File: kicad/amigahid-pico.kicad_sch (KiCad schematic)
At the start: 57 parts, among them J1 Amiga keyboard connector, J2 Conn_02x05_Top_Bottom, J3 Conn_02x05_Top_Bottom, J4 Conn_01x06, J5 Conn_01x04, Q1 BSS138, Q10 BSS138, Q11 BSS138, Q12 BSS138, Q13 BSS138, Q14 BSS138, Q15 BSS138, Q16 BSS138, Q17 BSS138, Q2 BSS138, Q3 BSS138, Q4 BSS138, Q5 BSS138, Q6 BSS138, Q7 BSS138, Q8 BSS138, Q9 BSS138, U1 Pico

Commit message: change resistor footprints to 1608 (metric)
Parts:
- R1, R10, R11, R12, R13, R14, R15, R16, R17, R18, R19, R2, R20, R21, R22, R23, R24, R25, R26, R27, R28, R29, R3, R30, R31, R32, R33, R34, R4, R5, R6, R7, R8, R9: footprint Resistor_SMD:R_0201_0603Metric -> Resistor_SMD:R_0603_1608Metric

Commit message: pcb rev 4
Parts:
- removed J2, J3: Conn_02x05_Top_Bottom, Connector_IDC:IDC-Header_2x05_P2.54mm_Vertical, symbol Connector_Generic:Conn_02x05_Top_Bottom
- removed J4: Conn_01x06, Connector_PinHeader_2.54mm:PinHeader_1x06_P2.54mm_Horizontal, symbol Connector_Generic:Conn_01x06
- removed J5: Conn_01x04, Connector_PinSocket_2.54mm:PinSocket_1x04_P2.54mm_Vertical, symbol Connector_Generic:Conn_01x04
- added J2: Debug/programming, Connector_PinHeader_2.54mm:PinHeader_1x06_P2.54mm_Horizontal, symbol Connector_Generic:Conn_01x06
- added J3: i2c header, Connector_PinHeader_2.54mm:PinHeader_1x04_P2.54mm_Vertical, symbol Connector_Generic:Conn_01x04
- added J4: USB_A, Connector_USB:USB_A_Molex_67643_Horizontal, symbol Connector:USB_A
- added J5: Controller 1, Connector_IDC:IDC-Header_2x05_P2.54mm_Vertical, symbol Connector_Generic:Conn_02x05_Odd_Even
- added J6: Controller 2, Connector_IDC:IDC-Header_2x05_P2.54mm_Vertical, symbol Connector_Generic:Conn_02x05_Odd_Even
- J1: value Amiga keyboard connector -> Amiga Keyboard
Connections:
- net +5V: now also R1.2, R11.2, R13.2, R15.2, R17.2, R19.2, R21.2, R23.2, R25.2, R27.2, R29.2, R3.2, R31.2, R33.2, R5.2, R7.2, R9.2, J4.1 (VBUS); no longer R1.1, R10.1, R12.1, R14.1, R16.1, R18.1, R20.1, R22.1, R24.1, R26.1, R28.1, R3.1, R30.1, R32.1, R34.1, R5.1, R8.1
- net kbclock: now reaches J1.1 (Pin_1), Q1.3 (D)
- net kbclock: now also R1.1; no longer R1.2
- net kbdata: now reaches J1.2 (Pin_2), Q2.3 (D)
- net kbdata: now also R3.1; no longer R3.2
- net kbreset: now reaches J1.3 (Pin_3), Q3.3 (D)
- net kbreset: now also R5.1; no longer R5.2
- net GND: now reaches J1.6 (Pin_6), U1.13 (GND), U1.18 (GND), U1.23 (GND), U1.28 (GND), U1.3 (GND), U1.33 (AGND), U1.38 (GND), U1.42 (GND), U1.8 (GND)
- net GND: now also J2.1 (Pin_1), J2.5 (Pin_5), J3.2 (Pin_2), J4.4 (GND), J4.5 (Shield), J5.6 (Pin_6), J6.6 (Pin_6)
- net kbpowerled: now reaches J1.7 (Pin_7)
- net kbdriveled: now reaches J1.8 (Pin_8)
- net uart tx: now reaches U1.1 (GPIO0)
- net uart tx: now also J2.2 (Pin_2)
- net lcont1 b3: now reaches U1.17 (GPIO13)
- net lcont1 b3: now also Q10.2 (S), R20.1
- net uart rx: now reaches U1.2 (GPIO1)
- net uart rx: now also J2.3 (Pin_3)
- net lcont2 h: now reaches U1.30 (RUN)
- net lcont2 h: now also Q12.2 (S), R24.1
- net +3V3: now reaches Q1.1 (G), Q10.1 (G), Q11.1 (G), Q12.1 (G), Q13.1 (G), Q14.1 (G), Q15.1 (G), Q16.1 (G), Q17.1 (G), Q2.1 (G), Q3.1 (G), Q4.1 (G), Q5.1 (G), Q6.1 (G), Q7.1 (G), Q8.1 (G), Q9.1 (G), U1.36 (3V3)
- net +3V3: now also R10.2, R12.2, R14.2, R16.2, R18.2, R2.2, R20.2, R22.2, R24.2, R26.2, R28.2, R30.2, R32.2, R34.2, R4.2, R6.2, R8.2, J3.1 (Pin_1); no longer R11.1, R13.1, R15.1, R17.1, R19.1, R2.1, R21.1, R23.1, R25.1, R27.1, R29.1, R31.1, R33.1, R4.1, R6.1, R7.1, R9.1
- net i2c sda: now reaches U1.4 (GPIO2)
- net i2c sda: now also J3.4 (Pin_4)
- net swclk: now reaches U1.41 (SWCLK)
- net swclk: now also J2.6 (Pin_6)
- net swdio: now reaches U1.43 (SWDIO)
- net swdio: now also J2.4 (Pin_4)
- net i2c scl: now reaches U1.5 (GPIO3)
- net i2c scl: now also J3.3 (Pin_3)
- net lkbreset: now reaches U1.6 (GPIO4)
- net lkbreset: now also Q3.2 (S), R6.1
- net lkbdata: now reaches U1.7 (GPIO5)
- net lkbdata: now also Q2.2 (S), R4.1
- net cont2 v: now reaches Q11.3 (D)
- net cont2 v: now also R21.1, J6.1 (Pin_1); no longer R22.2
- net cont2 b1: now reaches Q15.3 (D)
- net cont2 b1: now also R29.1, J6.2 (Pin_2); no longer R30.2
- net cont2 b2: now reaches Q16.3 (D)
- net cont2 b2: now also R31.1, J6.8 (Pin_8); no longer R32.2
- net cont1 b1: now reaches Q8.3 (D)
- net cont1 b1: now also R15.1, J5.2 (Pin_2); no longer R16.2
- net cont1 v: now reaches Q7.3 (D)
- net cont1 v: now also R13.1, J5.1 (Pin_1); no longer R14.2
- net cont1 h: now reaches Q6.3 (D)
- net cont1 h: now also R11.1, J5.3 (Pin_3); no longer R12.2
- net cont1 vq: now reaches Q5.3 (D)
- net cont1 vq: now also R9.1, J5.5 (Pin_5); no longer R10.2
- net cont1 hq: now reaches Q4.3 (D)
- net cont1 hq: now also R7.1, J5.7 (Pin_7); no longer R8.2
- net cont1 b2: now reaches Q9.3 (D)
- net cont1 b2: now also R17.1, J5.8 (Pin_8); no longer R18.2
- net cont1 b3: now reaches Q10.3 (D)
- net cont1 b3: now also R19.1, J5.9 (Pin_9); no longer R20.2
- net cont2 h: now reaches Q12.3 (D)
- net cont2 h: now also R23.1, J6.3 (Pin_3); no longer R24.2
- net cont2 b3: now reaches Q17.3 (D)
- net cont2 b3: now also R33.1, J6.9 (Pin_9); no longer R34.2
- net cont2 vq: now reaches Q13.3 (D)
- net cont2 vq: now also R25.1, J6.5 (Pin_5); no longer R26.2
- net cont2 hq: now reaches Q14.3 (D)
- net cont2 hq: now also R27.1, J6.7 (Pin_7); no longer R28.2
- new net lcont1 b1: Q8.2 (S), R16.1, U1.15 (GPIO11)
- new net lcont1 b2: Q9.2 (S), R18.1, U1.16 (GPIO12)
- new net lcont1 h: Q6.2 (S), R12.1, U1.12 (GPIO9)
- new net lcont1 hq: Q4.2 (S), R8.1, U1.10 (GPIO7)
- new net lcont1 v: Q7.2 (S), R14.1, U1.14 (GPIO10)
- new net lcont1 vq: Q5.2 (S), R10.1, U1.11 (GPIO8)
- new net lcont2 b1: Q15.2 (S), R30.1, U1.26 (GPIO20)
- new net lcont2 b2: Q16.2 (S), R32.1, U1.25 (GPIO19)
- new net lcont2 b3: Q17.2 (S), R34.1, U1.24 (GPIO18)
- new net lcont2 hq: Q14.2 (S), R28.1, U1.27 (GPIO21)
- new net lcont2 v: Q11.2 (S), R22.1, U1.31 (GPIO26_ADC0)
- new net lcont2 vq: Q13.2 (S), R26.1, U1.29 (GPIO22)
- new net lkbclock: Q1.2 (S), R2.1, U1.9 (GPIO6)
- new net usb d+: J4.3 (D+)
- new net usb d-: J4.2 (D-)
- now unconnected: U1.21 (GPIO16), U1.22 (GPIO17), U1.32 (GPIO27_ADC1), U1.34 (GPIO28_ADC2)
- no-connect marks 16 -> 14
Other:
- note added: "Amiga controller port (D-Sub 9, socket at peripheral side) pin m j 1 V UP 2 H DN 3 VQ LF 4 HQ RT 5 b3 b3 6 b1 b1 7 +5V +5V 8 GND GND 9 b2 b2 (n.b. idc ports are interleaved; d-subs are numbered top row, bottom row)"
- note added: "Controller 1 level conversion"
- note added: "Controller 2 level conversion"
- note added: "I/O Ports"
- note added: "Keyboard level conversion"
- note added: "MCU Section"
- note removed: "1 CLK 2 DAT 3 RES 4 +5V 5 n/c 6 GND 7 PWR 8 DRV"
- note removed: "Amiga controller port pin m j 1 V UP 2 H DN 3 VQ LF 4 HQ RT 5 b3 b3 6 b1 b1 7 +5V +5V 8 GND GND 9 b2 b2"
- note removed: "Debug & Programming Header (optional) 6 swclk 5 swdio gnd 4 swdio 3 uart rx 2 uart tx 1 uart gnd"
- note removed: "Pico signal reference signal gpio pin mouse vq gp6 9 mouse hq gp7 10 mouse v gp8 11 mouse h gp9 12 kbreset gp10 14 kbdata gp11 15 kbclock gp12 16 mouse b1 gp22 29 mouse b2 gp26 31 mouse b3 gp27 32"
- note removed: "controller port 1"
- note removed: "controller port 2"
- note removed: "i2c display 1 VCC (3v3) 2 GND 3 SCL 4 SDA"
- note removed: "keyboard level conversion"

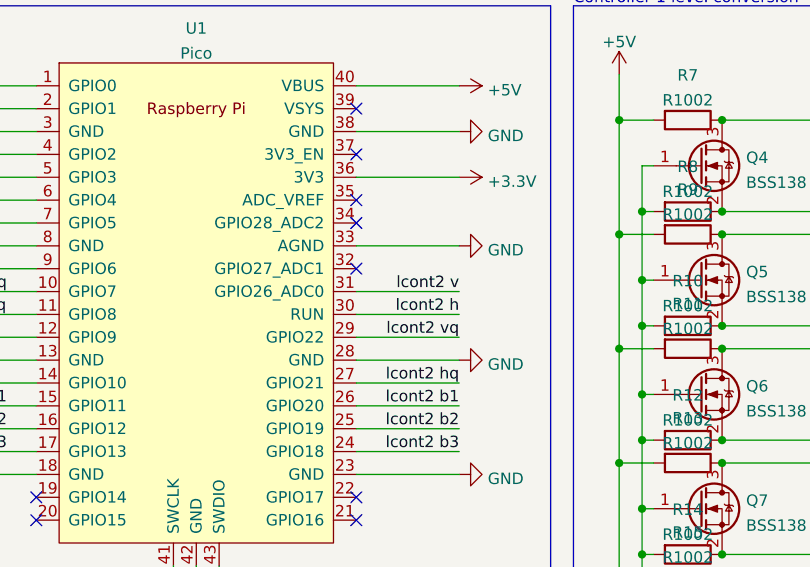
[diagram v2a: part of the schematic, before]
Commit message: revision 5 pcb (fixes #17 and #18)
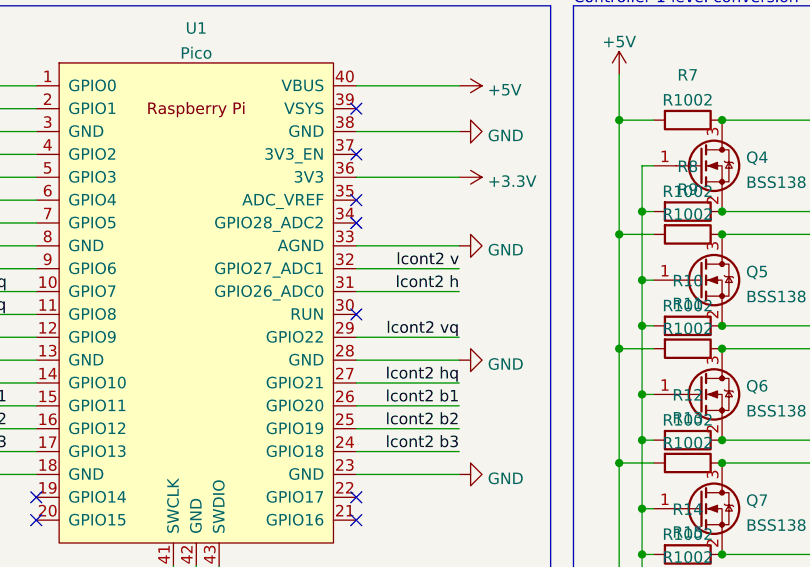
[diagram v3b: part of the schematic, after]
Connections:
- net lcont2 h: now also U1.31 (GPIO26_ADC0); no longer U1.30 (RUN)
- net lcont2 v: now also U1.32 (GPIO27_ADC1); no longer U1.31 (GPIO26_ADC0)
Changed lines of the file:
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@@
   (title_block
     (title "amiga keyboard adapter")
-    (date "2022-04-10")
-    (rev "4")
+    (date "2022-04-21")
+    (rev "5")
     (comment 2 "please note: design uses fets in place of ic")
     (comment 4 "debug & programming header, display header optional")
@@
   (no_connect (at 124.46 76.2))
   (no_connect (at 54.61 78.74))
+  (no_connect (at 160.02 55.88))
   (no_connect (at 54.61 86.36))
-  (no_connect (at 160.02 50.8))
   (no_connect (at 160.02 45.72))
   (no_connect (at 160.02 76.2))
@@
     (stroke (width 0) (type default) (color 0 0 0 0))
   )
+  (wire (pts (xy 171.45 50.8) (xy 160.02 50.8))
+    (stroke (width 0) (type default) (color 0 0 0 0))
+  )
+  (wire (pts (xy 54.61 64.77) (xy 63.5 64.77))
+    (stroke (width 0) (type default) (color 0 0 0 0))
+  )
+  (wire (pts (xy 113.03 60.96) (xy 124.46 60.96))
+    (stroke (width 0) (type default) (color 0 0 0 0))
+  )
+  (wire (pts (xy 238.76 107.95) (xy 238.76 115.57))
+    (stroke (width 0) (type default) (color 0 0 0 0))
+  )
+  (wire (pts (xy 144.78 142.24) (xy 144.78 147.32))
+    (stroke (width 0) (type default) (color 0 0 0 0))
+  )
+  (polyline (pts (xy 228.6 21.59) (xy 228.6 133.35))
+    (stroke (width 0) (type default) (color 0 0 0 0))
+  )
+  (wire (pts (xy 200.66 85.09) (xy 223.52 85.09))
+    (stroke (width 0) (type default) (color 0 0 0 0))
+  )
+  (polyline (pts (xy 31.75 95.25) (xy 31.75 21.59))
+    (stroke (width 0) (type default) (color 0 0 0 0))
+  )
+  (wire (pts (xy 247.65 59.69) (xy 270.51 59.69))
+    (stroke (width 0) (type default) (color 0 0 0 0))
+  )
+  (wire (pts (xy 144.78 121.92) (xy 146.05 121.92))
+    (stroke (width 0) (type default) (color 0 0 0 0))
+  )
+  (wire (pts (xy 191.77 95.25) (xy 193.04 95.25))
+    (stroke (width 0) (type default) (color 0 0 0 0))
+  )
+  (wire (pts (xy 171.45 40.64) (xy 160.02 40.64))
+    (stroke (width 0) (type default) (color 0 0 0 0))
+  )
+  (wire (pts (xy 74.93 46.99) (xy 82.55 46.99))
+    (stroke (width 0) (type default) (color 0 0 0 0))
+  )
+  (wire (pts (xy 191.77 90.17) (xy 191.77 95.25))
+    (stroke (width 0) (type default) (color 0 0 0 0))
+  )
+  (wire (pts (xy 191.77 102.87) (xy 193.04 102.87))
+    (stroke (width 0) (type default) (color 0 0 0 0))
+  )
+  (polyline (pts (xy 181.61 99.06) (xy 181.61 160.02))
+    (stroke (width 0) (type default) (color 0 0 0 0))
+  )
+  (wire (pts (xy 191.77 115.57) (xy 191.77 120.65))
+    (stroke (width 0) (type default) (color 0 0 0 0))
+  )
+  (wire (pts (xy 238.76 120.65) (xy 240.03 120.65))
+    (stroke (width 0) (type default) (color 0 0 0 0))
+  )
+  (wire (pts (xy 238.76 90.17) (xy 238.76 95.25))
+    (stroke (width 0) (type default) (color 0 0 0 0))
+  )
+  (wire (pts (xy 48.26 41.91) (xy 60.96 41.91))
+    (stroke (width 0) (type default) (color 0 0 0 0))
+  )
   (wire (pts (xy 171.45 53.34) (xy 160.02 53.34))
-    (stroke (width 0) (type default) (color 0 0 0 0))
-  )
-  (wire (pts (xy 54.61 64.77) (xy 63.5 64.77))
-    (stroke (width 0) (type default) (color 0 0 0 0))
-  )
-  (wire (pts (xy 113.03 60.96) (xy 124.46 60.96))
-    (stroke (width 0) (type default) (color 0 0 0 0))
-  )
-  (wire (pts (xy 238.76 107.95) (xy 238.76 115.57))
-    (stroke (width 0) (type default) (color 0 0 0 0))
-  )
-  (wire (pts (xy 144.78 142.24) (xy 144.78 147.32))
-    (stroke (width 0) (type default) (color 0 0 0 0))
-  )
-  (polyline (pts (xy 228.6 21.59) (xy 228.6 133.35))
-    (stroke (width 0) (type default) (color 0 0 0 0))
-  )
-  (wire (pts (xy 200.66 85.09) (xy 223.52 85.09))
-    (stroke (width 0) (type default) (color 0 0 0 0))
-  )
-  (polyline (pts (xy 31.75 95.25) (xy 31.75 21.59))
-    (stroke (width 0) (type default) (color 0 0 0 0))
-  )
-  (wire (pts (xy 247.65 59.69) (xy 270.51 59.69))
-    (stroke (width 0) (type default) (color 0 0 0 0))
-  )
-  (wire (pts (xy 144.78 121.92) (xy 146.05 121.92))
-    (stroke (width 0) (type default) (color 0 0 0 0))
-  )
-  (wire (pts (xy 191.77 95.25) (xy 193.04 95.25))
-    (stroke (width 0) (type default) (color 0 0 0 0))
-  )
-  (wire (pts (xy 171.45 40.64) (xy 160.02 40.64))
-    (stroke (width 0) (type default) (color 0 0 0 0))
-  )
-  (wire (pts (xy 74.93 46.99) (xy 82.55 46.99))
-    (stroke (width 0) (type default) (color 0 0 0 0))
-  )
-  (wire (pts (xy 191.77 90.17) (xy 191.77 95.25))
-    (stroke (width 0) (type default) (color 0 0 0 0))
-  )
-  (wire (pts (xy 191.77 102.87) (xy 193.04 102.87))
-    (stroke (width 0) (type default) (color 0 0 0 0))
-  )
-  (polyline (pts (xy 181.61 99.06) (xy 181.61 160.02))
-    (stroke (width 0) (type default) (color 0 0 0 0))
-  )
-  (wire (pts (xy 191.77 115.57) (xy 191.77 120.65))
-    (stroke (width 0) (type default) (color 0 0 0 0))
-  )
-  (wire (pts (xy 238.76 120.65) (xy 240.03 120.65))
-    (stroke (width 0) (type default) (color 0 0 0 0))
-  )
-  (wire (pts (xy 238.76 90.17) (xy 238.76 95.25))
-    (stroke (width 0) (type default) (color 0 0 0 0))
-  )
-  (wire (pts (xy 48.26 41.91) (xy 60.96 41.91))
-    (stroke (width 0) (type default) (color 0 0 0 0))
-  )
-  (wire (pts (xy 171.45 55.88) (xy 160.02 55.88))
     (stroke (width 0) (type default) (color 0 0 0 0))
   )
@@
     (effects (font (size 1.27 1.27)) (justify right bottom))
   )
-  (label "lcont2 h" (at 171.45 55.88 180)
-    (effects (font (size 1.27 1.27)) (justify right bottom))
-  )
-  (label "lcont2 v" (at 171.45 53.34 180)
-    (effects (font (size 1.27 1.27)) (justify right bottom))
-  )
+  (label "lcont2 h" (at 171.45 53.34 180)
+    (effects (font (size 1.27 1.27)) (justify right bottom))
+  )
+  (label "lcont2 v" (at 171.45 50.8 180)
+    (effects (font (size 1.27 1.27)) (justify right bottom))
+  )
